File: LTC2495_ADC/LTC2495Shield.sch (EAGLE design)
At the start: 14 parts

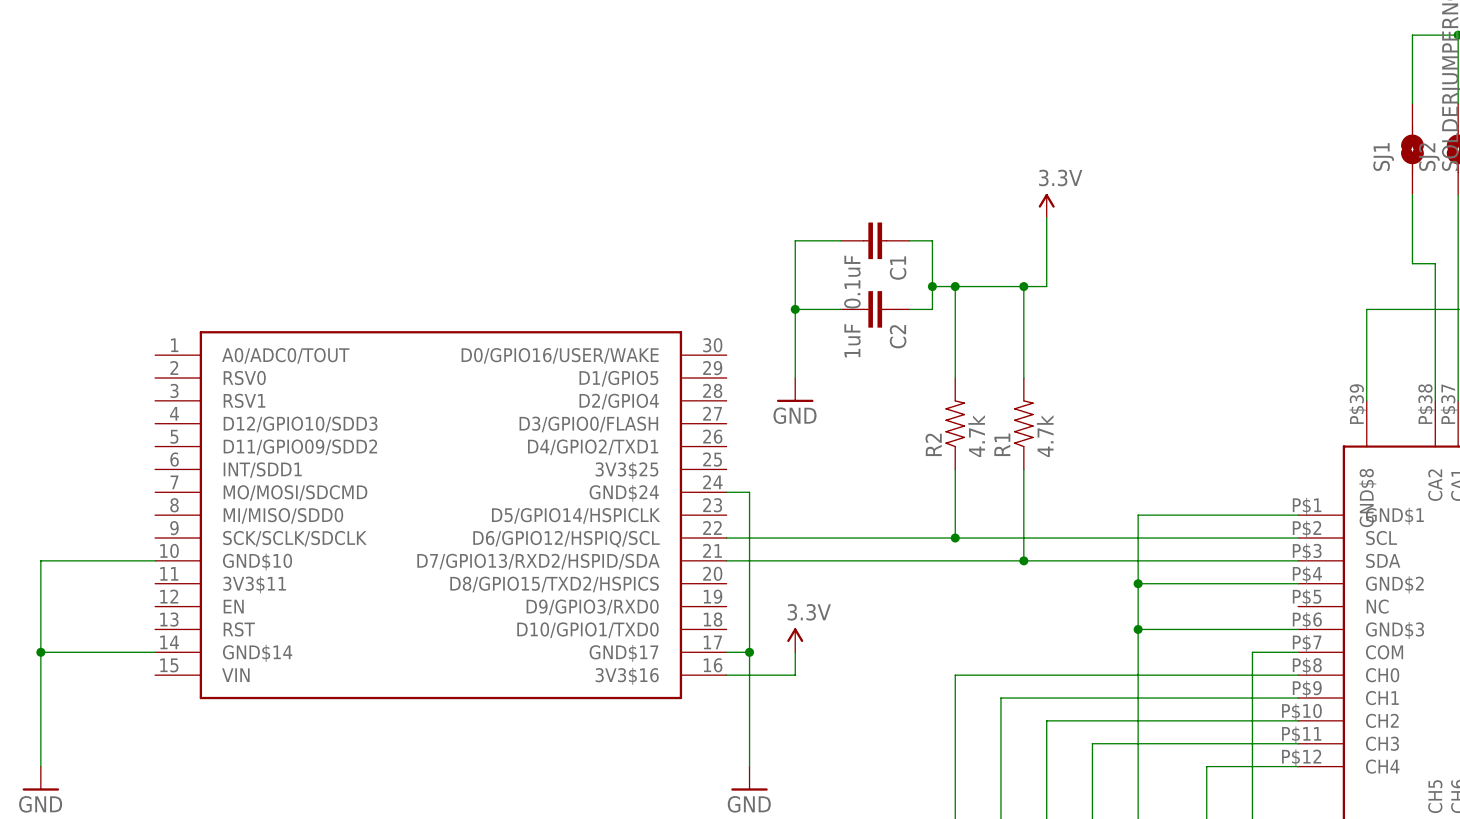
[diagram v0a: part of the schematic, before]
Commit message: Updated the i2c pins to all shields to use d11/d12  as these pins will have dual use with the upcoming wifimcu Added FM24W256  Fram shield Added X95840 Digital potentiometer Shield Added AD5696 DAC Shield
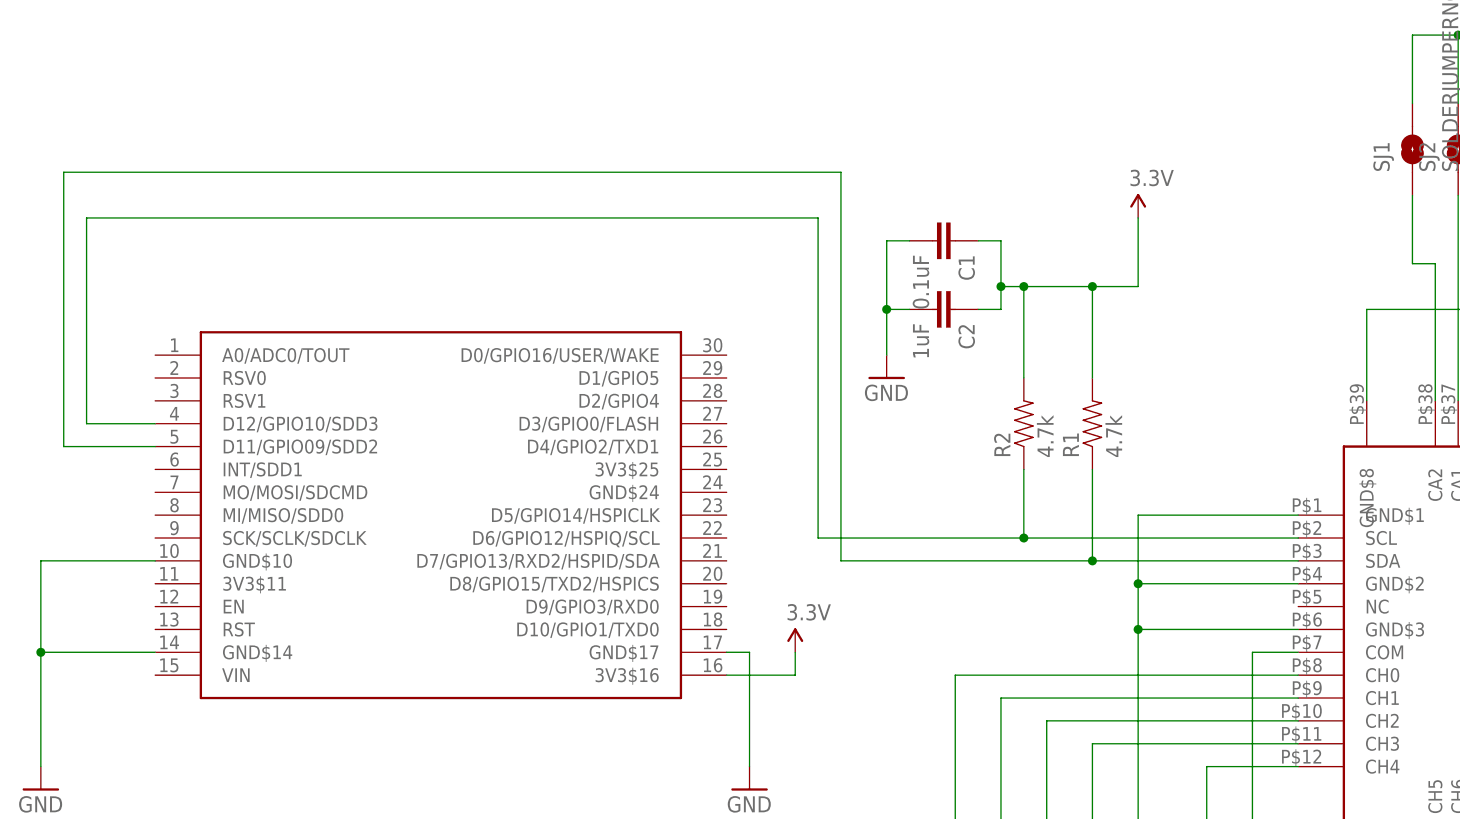
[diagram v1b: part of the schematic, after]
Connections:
- net GND: no longer U$1.GND$24
- net N$2: now also U$1.D11/GPIO09/SDD2; no longer U$1.D7/GPIO13/RXD2/HSPID/SDA
- net N$8: now also U$1.D12/GPIO10/SDD3; no longer U$1.D6/GPIO12/HSPIQ/SCL
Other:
- moved on the sheet: C1, C2, R1, R2
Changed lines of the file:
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@@
 <instance part="U$1" gate="G$1" x="25.4" y="48.26"/>
 <instance part="GND1" gate="1" x="-5.08" y="17.78"/>
-<instance part="GND2" gate="1" x="78.74" y="60.96"/>
+<instance part="GND2" gate="1" x="88.9" y="63.5"/>
 <instance part="P+1" gate="G$1" x="78.74" y="33.02"/>
-<instance part="R1" gate="G$1" x="104.14" y="58.42" rot="R90"/>
-<instance part="R2" gate="G$1" x="96.52" y="58.42" rot="R90"/>
-<instance part="C1" gate="G$1" x="86.36" y="78.74" rot="R270"/>
-<instance part="P+3" gate="G$1" x="106.68" y="81.28"/>
-<instance part="C2" gate="G$1" x="86.36" y="71.12" rot="R270"/>
+<instance part="R1" gate="G$1" x="111.76" y="58.42" rot="R90"/>
+<instance part="R2" gate="G$1" x="104.14" y="58.42" rot="R90"/>
+<instance part="C1" gate="G$1" x="93.98" y="78.74" rot="R270"/>
+<instance part="P+3" gate="G$1" x="116.84" y="81.28"/>
+<instance part="C2" gate="G$1" x="93.98" y="71.12" rot="R270"/>
 <instance part="GND3" gate="1" x="116.84" y="5.08"/>
 <instance part="U$3" gate="G$1" x="144.78" y="20.32"/>
@@
 <pinref part="C1" gate="G$1" pin="2"/>
 <pinref part="GND2" gate="1" pin="GND"/>
-<wire x1="83.82" y1="78.74" x2="78.74" y2="78.74" width="0.1524" layer="91"/>
-<wire x1="78.74" y1="78.74" x2="78.74" y2="71.12" width="0.1524" layer="91"/>
+<wire x1="91.44" y1="78.74" x2="88.9" y2="78.74" width="0.1524" layer="91"/>
+<wire x1="88.9" y1="78.74" x2="88.9" y2="71.12" width="0.1524" layer="91"/>
 <pinref part="C2" gate="G$1" pin="2"/>
-<wire x1="78.74" y1="71.12" x2="78.74" y2="63.5" width="0.1524" layer="91"/>
-<wire x1="83.82" y1="71.12" x2="78.74" y2="71.12" width="0.1524" layer="91"/>
-<junction x="78.74" y="71.12"/>
+<wire x1="88.9" y1="71.12" x2="88.9" y2="66.04" width="0.1524" layer="91"/>
+<wire x1="91.44" y1="71.12" x2="88.9" y2="71.12" width="0.1524" layer="91"/>
+<junction x="88.9" y="71.12"/>
 </segment>
 <segment>
@@
 <wire x1="71.12" y1="33.02" x2="73.66" y2="33.02" width="0.1524" layer="91"/>
 <wire x1="73.66" y1="33.02" x2="73.66" y2="20.32" width="0.1524" layer="91"/>
-<pinref part="U$1" gate="G$1" pin="GND$24"/>
-<wire x1="71.12" y1="50.8" x2="73.66" y2="50.8" width="0.1524" layer="91"/>
-<wire x1="73.66" y1="50.8" x2="73.66" y2="33.02" width="0.1524" layer="91"/>
-<junction x="73.66" y="33.02"/>
 </segment>
 </net>
@@
 <segment>
 <pinref part="R2" gate="G$1" pin="2"/>
-<wire x1="96.52" y1="63.5" x2="96.52" y2="73.66" width="0.1524" layer="91"/>
+<wire x1="104.14" y1="63.5" x2="104.14" y2="73.66" width="0.1524" layer="91"/>
 <pinref part="P+3" gate="G$1" pin="3.3V"/>
-<wire x1="96.52" y1="73.66" x2="104.14" y2="73.66" width="0.1524" layer="91"/>
-<wire x1="104.14" y1="73.66" x2="106.68" y2="73.66" width="0.1524" layer="91"/>
-<wire x1="106.68" y1="73.66" x2="106.68" y2="81.28" width="0.1524" layer="91"/>
+<wire x1="104.14" y1="73.66" x2="111.76" y2="73.66" width="0.1524" layer="91"/>
+<wire x1="111.76" y1="73.66" x2="116.84" y2="73.66" width="0.1524" layer="91"/>
+<wire x1="116.84" y1="73.66" x2="116.84" y2="81.28" width="0.1524" layer="91"/>
 <pinref part="R1" gate="G$1" pin="2"/>
-<wire x1="104.14" y1="63.5" x2="104.14" y2="73.66" width="0.1524" layer="91"/>
+<wire x1="111.76" y1="63.5" x2="111.76" y2="73.66" width="0.1524" layer="91"/>
+<junction x="111.76" y="73.66"/>
+<wire x1="104.14" y1="73.66" x2="101.6" y2="73.66" width="0.1524" layer="91"/>
+<wire x1="101.6" y1="73.66" x2="101.6" y2="78.74" width="0.1524" layer="91"/>
 <junction x="104.14" y="73.66"/>
-<wire x1="96.52" y1="73.66" x2="93.98" y2="73.66" width="0.1524" layer="91"/>
-<wire x1="93.98" y1="73.66" x2="93.98" y2="78.74" width="0.1524" layer="91"/>
-<junction x="96.52" y="73.66"/>
 <pinref part="C1" gate="G$1" pin="1"/>
-<wire x1="93.98" y1="78.74" x2="91.44" y2="78.74" width="0.1524" layer="91"/>
-<wire x1="93.98" y1="73.66" x2="93.98" y2="71.12" width="0.1524" layer="91"/>
-<junction x="93.98" y="73.66"/>
+<wire x1="101.6" y1="78.74" x2="99.06" y2="78.74" width="0.1524" layer="91"/>
+<wire x1="101.6" y1="73.66" x2="101.6" y2="71.12" width="0.1524" layer="91"/>
+<junction x="101.6" y="73.66"/>
 <pinref part="C2" gate="G$1" pin="1"/>
-<wire x1="93.98" y1="71.12" x2="91.44" y2="71.12" width="0.1524" layer="91"/>
+<wire x1="101.6" y1="71.12" x2="99.06" y2="71.12" width="0.1524" layer="91"/>
 </segment>
 <segment>
@@
 <net name="N$2" class="0">
 <segment>
-<pinref part="U$1" gate="G$1" pin="D7/GPIO13/RXD2/HSPID/SDA"/>
-<wire x1="134.62" y1="43.18" x2="104.14" y2="43.18" width="0.1524" layer="91"/>
+<wire x1="134.62" y1="43.18" x2="111.76" y2="43.18" width="0.1524" layer="91"/>
 <pinref part="R1" gate="G$1" pin="1"/>
-<wire x1="104.14" y1="43.18" x2="71.12" y2="43.18" width="0.1524" layer="91"/>
-<wire x1="104.14" y1="53.34" x2="104.14" y2="43.18" width="0.1524" layer="91"/>
-<junction x="104.14" y="43.18"/>
+<wire x1="111.76" y1="43.18" x2="83.82" y2="43.18" width="0.1524" layer="91"/>
+<wire x1="111.76" y1="53.34" x2="111.76" y2="43.18" width="0.1524" layer="91"/>
+<junction x="111.76" y="43.18"/>
 <pinref part="U$3" gate="G$1" pin="SDA"/>
+<pinref part="U$1" gate="G$1" pin="D11/GPIO09/SDD2"/>
+<wire x1="7.62" y1="55.88" x2="-2.54" y2="55.88" width="0.1524" layer="91"/>
+<wire x1="-2.54" y1="55.88" x2="-2.54" y2="86.36" width="0.1524" layer="91"/>
+<wire x1="-2.54" y1="86.36" x2="83.82" y2="86.36" width="0.1524" layer="91"/>
+<wire x1="83.82" y1="86.36" x2="83.82" y2="43.18" width="0.1524" layer="91"/>
 </segment>
 </net>
 <net name="N$8" class="0">
 <segment>
-<pinref part="U$1" gate="G$1" pin="D6/GPIO12/HSPIQ/SCL"/>
-<wire x1="134.62" y1="45.72" x2="96.52" y2="45.72" width="0.1524" layer="91"/>
+<wire x1="134.62" y1="45.72" x2="104.14" y2="45.72" width="0.1524" layer="91"/>
 <pinref part="R2" gate="G$1" pin="1"/>
-<wire x1="96.52" y1="45.72" x2="71.12" y2="45.72" width="0.1524" layer="91"/>
-<wire x1="96.52" y1="53.34" x2="96.52" y2="45.72" width="0.1524" layer="91"/>
-<junction x="96.52" y="45.72"/>
+<wire x1="104.14" y1="45.72" x2="81.28" y2="45.72" width="0.1524" layer="91"/>
+<wire x1="104.14" y1="53.34" x2="104.14" y2="45.72" width="0.1524" layer="91"/>
+<junction x="104.14" y="45.72"/>
 <pinref part="U$3" gate="G$1" pin="SCL"/>
+<wire x1="81.28" y1="45.72" x2="81.28" y2="81.28" width="0.1524" layer="91"/>
+<wire x1="81.28" y1="81.28" x2="0" y2="81.28" width="0.1524" layer="91"/>
+<wire x1="0" y1="81.28" x2="0" y2="58.42" width="0.1524" layer="91"/>
+<pinref part="U$1" gate="G$1" pin="D12/GPIO10/SDD3"/>
+<wire x1="0" y1="58.42" x2="7.62" y2="58.42" width="0.1524" layer="91"/>
 </segment>
 </net>
